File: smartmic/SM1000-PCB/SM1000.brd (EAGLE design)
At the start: 125 x 100 mm, 140 parts, among them CN1 HDR100-6, CN2 MOLEX-MINI-B-SMT, CN3 RASM712PX, CN4 RJ-45, CN5 MJ-3523-SMT, CN6 MJ-3523-SMT, CN7 MJ-3523-SMT, CN8 MJ-3523-SMT, CN9 MJ-3523-SMT, IC1 DIL-16, J1 JMP-2PIN, J2 JMP-2PIN, J3 JMP-2PIN, J4 JMP-2PIN, J5 JMP-2PIN, Q1 MMBT4401, Q2 MMBT4401, SW1 SW-SPST-2-1437565-0, SW2 SW-SPST-2-1437565-0, SW3 DPDT, T1 LM-NP-1001-B1L, T2 LM-NP-1001-B1L, U1 STM32F407, U2 LD3985M33R, U3 STMPS2141, U4 EMIF02-USB03F2, U5 TPS54329E, U6 LMV341, U7 LMV341, U8 LM386M-1, X1 8.0MHz

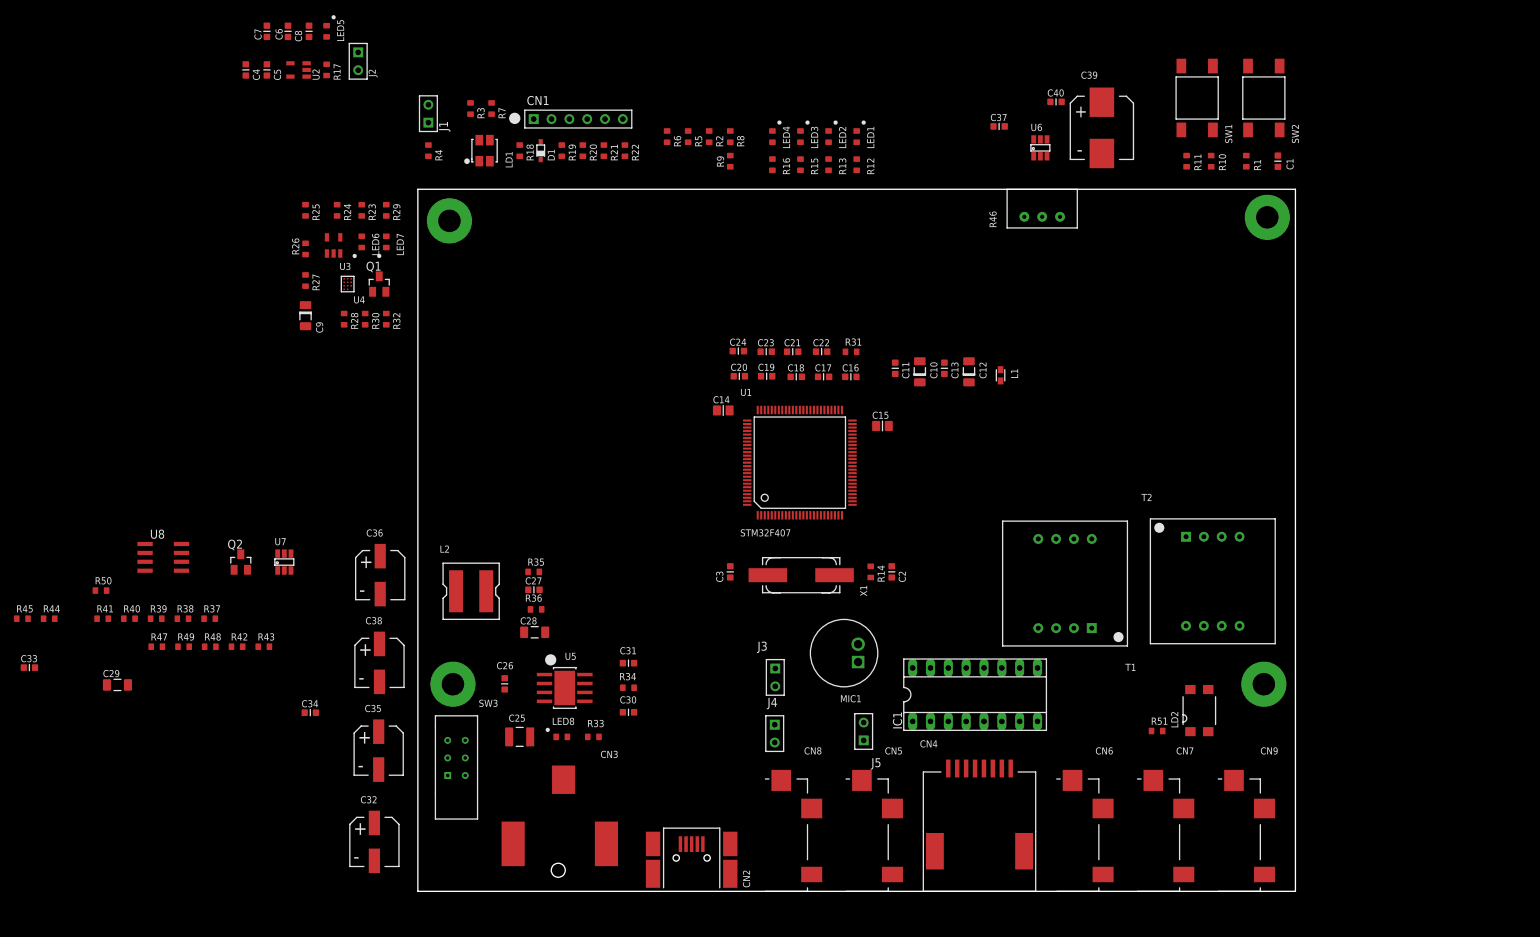
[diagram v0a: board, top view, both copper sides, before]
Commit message: 
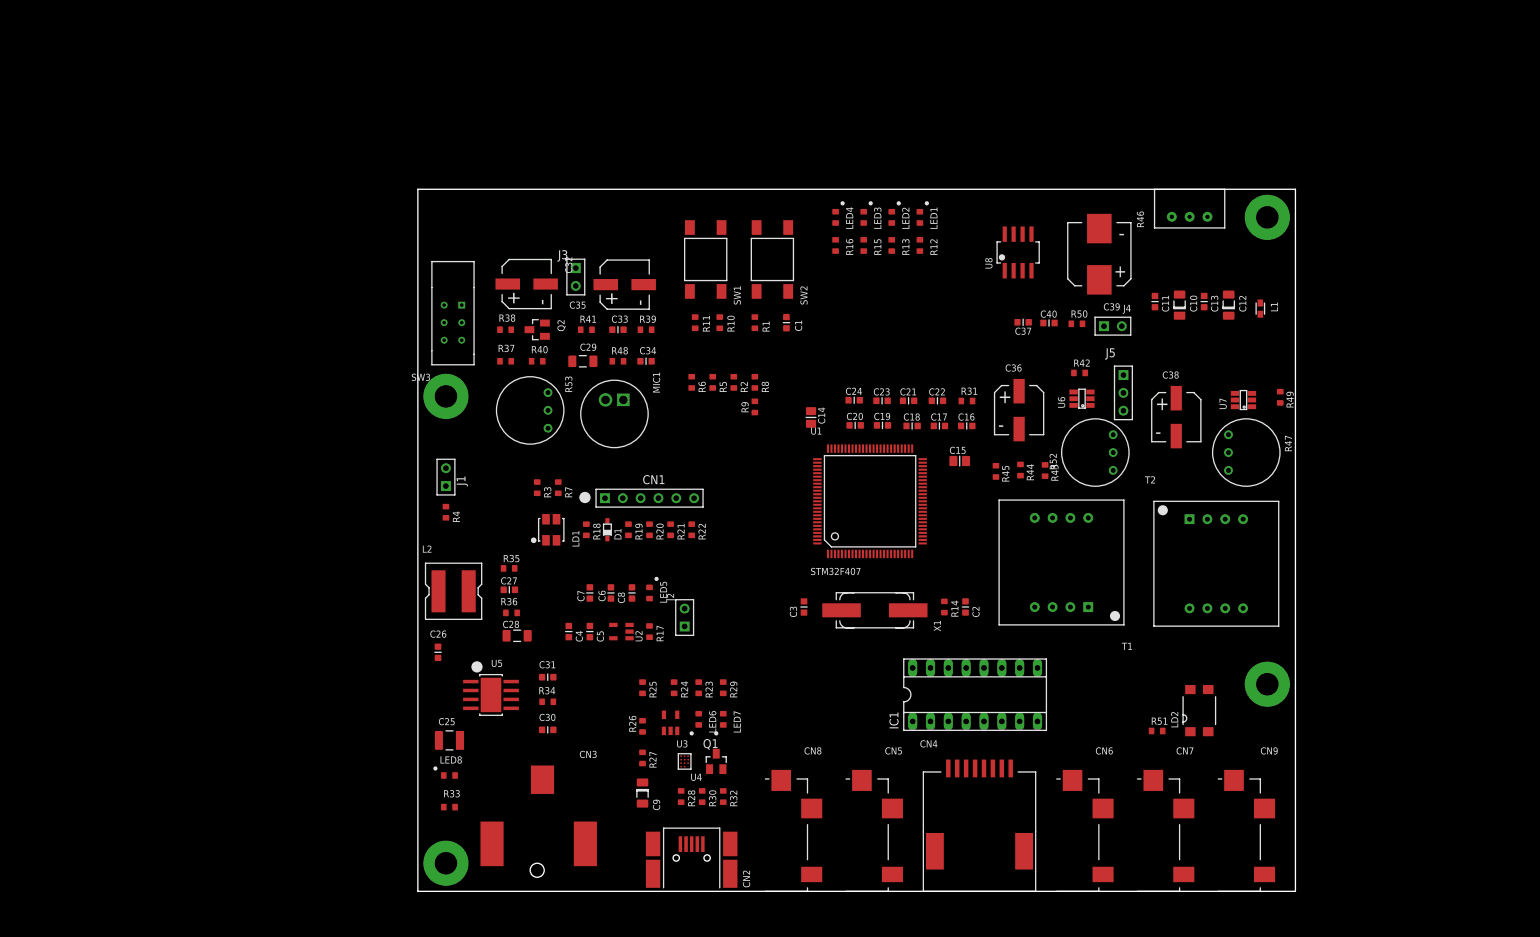
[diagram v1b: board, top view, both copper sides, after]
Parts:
- added R52: 10K, _RoweTel:TRIMPOT91
- added R53: TRIMPOT91, _RoweTel:TRIMPOT91
- added SH4: SHUNT,0.1IN, _Coherix:NOPACKAGE
- J5: value JMP-2PIN -> JMPR-3PIN; device _Coherix:JMPR-2PIN -> _Coherix:JMPR-3PIN
- LED1: value LED-GRN -> LED-RED
- LED2: value LED-ORG -> LED-RED
- LED3: value LED-RED -> LED-GRN
- LED4: value LED-BLU -> LED-YEL
- R42: value 4.99K,1% -> 10K,1%
- R47: value 100K,1% -> 100K; device _RoweTel:R0603 -> _RoweTel:TRIMPOT91
- U8: device AA-IC:SO08 -> _RoweTel:SO08
- moved R49 160.2 mm to (122.8, 70.4), turned to 270 degrees
- moved R47 157.6 mm to (118.0, 62.5), turned to 270 degrees
- moved R50 144.1 mm to (93.9, 80.8)
- moved R45 140.2 mm to (82.3, 59.8), turned to 270 degrees
- moved R44 140.0 mm to (85.8, 60.0), turned to 270 degrees
- moved U7 138.6 mm to (117.6, 70.0), turned to 90 degrees
- moved U8 129.3 mm to (85.5, 91.0), turned to 0 degrees
- moved R42 126.2 mm to (94.2, 73.8)
- moved C38 118.8 mm to (108.0, 67.5)
- moved R43 114.1 mm to (89.3, 59.9), turned to 270 degrees
- moved C33 96.7 mm to (28.5, 80.0), turned to 180 degrees
- moved C36 94.0 mm to (85.6, 68.5)
- moved J2 93.0 mm to (38.0, 39.0), turned to 180 degrees
- moved C4 92.3 mm to (21.5, 37.0)
- moved C5 92.3 mm to (24.5, 37.0)
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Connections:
- net LED-BLU renamed LED-ERR
- net LED-GRN renamed LED-PWR
- net LED-ORG renamed LED-PTT
- net LED-RED renamed LED-RT
- new net N$48: R42.1, R52.3, U6.4
- new net N$60: CN5.10, J5.2
- net AIN2: now also R52.2; no longer R42.1, U6.4
- net GND: now also J5.3, R52.1; no longer J5.2
- net N$32: no longer CN5.10
- net N$90: now also R47.3
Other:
- board text added: "AUX INP"
- board text added: "ERROR LED"
- board text added: "EXT MIC"
- board text added: "EXT SPKR"
- board text added: "EXT SPKR AMP"
- board text added: "MIC"
- board text added: "MIC INTF."
- board text added: "MIC PREAMP"
- board text added: "OTG USB"
- board text added: "PTT"
- board text added: "PTT LED"
- board text added: "PWR IN"
- board text added: "PWR LED"
- board text added: "PWR SW"
- board text added: "RCVR LEV"
- board text added: "SPEAKER INTF."
- board text added: "SPKR"
- board text added: "SPKR LEV"
- board text added: "USB INTF"

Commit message: SM1000
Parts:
- removed J4: JMP-2PIN, _Coherix:JMPR-2PIN
- added C41, C42, C43, C45: 100nF,16V, _RoweTel:C0603
- added C44: 100nf,16V, _RoweTel:C0603
- added FB1, FB2, FB3, FB4, FB6: FB0805, _RoweTel:FE0805
- added FB5: FB1210, _RoweTel:FE1210
- added R54: 1K,1%, _RoweTel:R0603
- C22, C23: device _Coherix:C0603 -> _RoweTel:C0603
- LED1, LED2, LED3, LED4: device _Coherix:CHIP-LED-0603 -> _RoweTel:LTST-S2200K
- R53: value TRIMPOT91 -> 10K
- T1, T2: value LM-NP-1001-B1L -> SM-LP-5001; device _RoweTel:LM-NP-1001-B1L -> _RoweTel:SM-LP-5001
- moved C22 83.3 mm to (-8.00, 55.0)
- moved C29 71.9 mm to (-13.0, 13.5)
- moved C32 71.9 mm to (-21.0, 24.5)
- moved C33 71.9 mm to (-8.00, 18.0)
- moved C34 71.9 mm to (-4.00, 13.5)
- moved C35 71.9 mm to (-7.04, 24.4)
- moved J3 71.9 mm to (-14.0, 25.5)
- moved MIC1 71.9 mm to (-8.50, 6.00)
- moved Q2 71.9 mm to (-19.5, 18.0)
- moved R37 71.9 mm to (-24.0, 13.5)
- moved R38 71.9 mm to (-24.0, 18.0)
- moved R39 71.9 mm to (-4.00, 18.0)
- moved R40 71.9 mm to (-19.5, 13.5)
- moved R41 71.9 mm to (-12.5, 18.0)
- moved R48 71.9 mm to (-8.00, 13.5)
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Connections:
- removed net N$37: C25.1, R33.1, R34.1, SW3.6, U5.2
- new net N$70: Q2.3, R38.2, R40.1, R53.1
- new net N$72: CN7.2, FB2.2
- new net N$73: CN9.2, FB6.2
- new net N$74: FB6.1, LD2.4
- new net N$75: CN8.2, FB3.2
- new net N$76: CN5.2, FB4.1
- new net N$77: CN3.2, FB5.1
- new net N$78: FB5.2, SW3.5
- net +3.3V: no longer LD1.4
- net +5V: now also C22.1
- net +VIN: now also C23.1, C25.1, R33.1, R34.1, SW3.6, U5.2; no longer CN3.2, SW3.5
- net AIN2: now also R53.2; no longer Q2.3, R38.2, R40.1
- net GND: now also C41.2, C42.2, R53.3, R54.1, T1.3, T2.3; no longer J4.1, T1.5, T2.4
- net MIC: now also C44.1
- net N$25: now also FB4.2; no longer CN5.2
- net N$33: now also FB1.1, T1.6; no longer CN6.2, T1.1
- net N$44: now also FB3.1; no longer CN8.2
- net N$61: now also FB2.1, T2.6; no longer CN7.2, T2.8
- net N$63: now also R54.2, T1.1; no longer T1.8
- net N$64: now also CN6.2, FB1.2; no longer CN8.10, J4.2
- net PTT: now also C45.1; no longer LD2.4
- net RF: now also C43.2, C44.2, C45.2, T2.4; no longer T2.5
- net SPKR: now also C43.1
- net VDD: now also C41.1, C42.1, LD1.4; no longer C22.1, C23.1
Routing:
- net PTT: track 0.00 -> 44.8 mm, vias 0 -> 2
- net MIC: track 0.00 -> 38.5 mm, vias 0 -> 1
- net SPKR: track 0.00 -> 37.0 mm, vias 0 -> 1
- net N$61: track 0.00 -> 19.2 mm, vias 0 -> 2
- net GND: track 0.00 -> 14.9 mm, vias 0 -> 3
- net N$33: track 0.00 -> 14.6 mm, vias 0 -> 2
- net N$73: track 0.00 -> 13.1 mm, vias 0 -> 2
- net N$72: track 0.00 -> 10.0 mm
- net N$64: track 0.00 -> 9.10 mm
- net N$51: track 0.00 -> 8.95 mm
- net N$58: track 0.00 -> 8.65 mm
- net STLINK: track 0.00 -> 8.17 mm
- net N$52: track 0.00 -> 7.84 mm
- net N$57: track 0.00 -> 6.96 mm
- net N$53: track 0.00 -> 6.14 mm
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- added copper zone on layer 1, net GND
- added copper zone on layer 15, net GND
- added copper zone on layer 1, net RF
- added copper zone on layer 2, net VDD
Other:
- board size 125 x 100 mm -> 100 x 80 mm
- board text removed: "EXT SPKR AMP"
- board text removed: "LED1-4"
- board text removed: "MIC PREAMP"

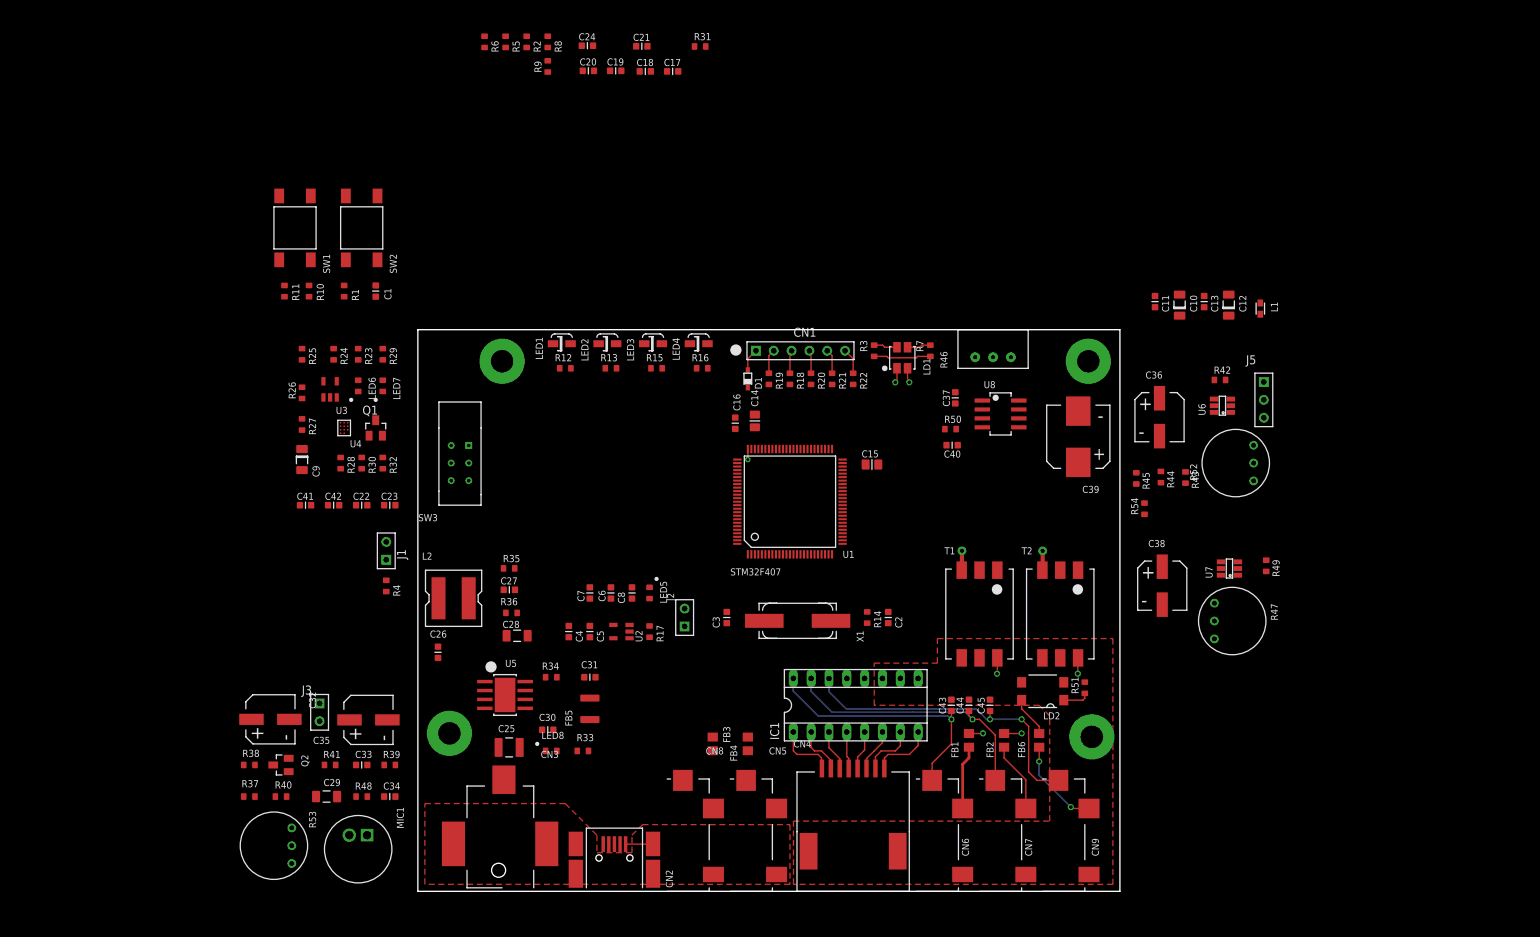
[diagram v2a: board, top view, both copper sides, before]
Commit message: 
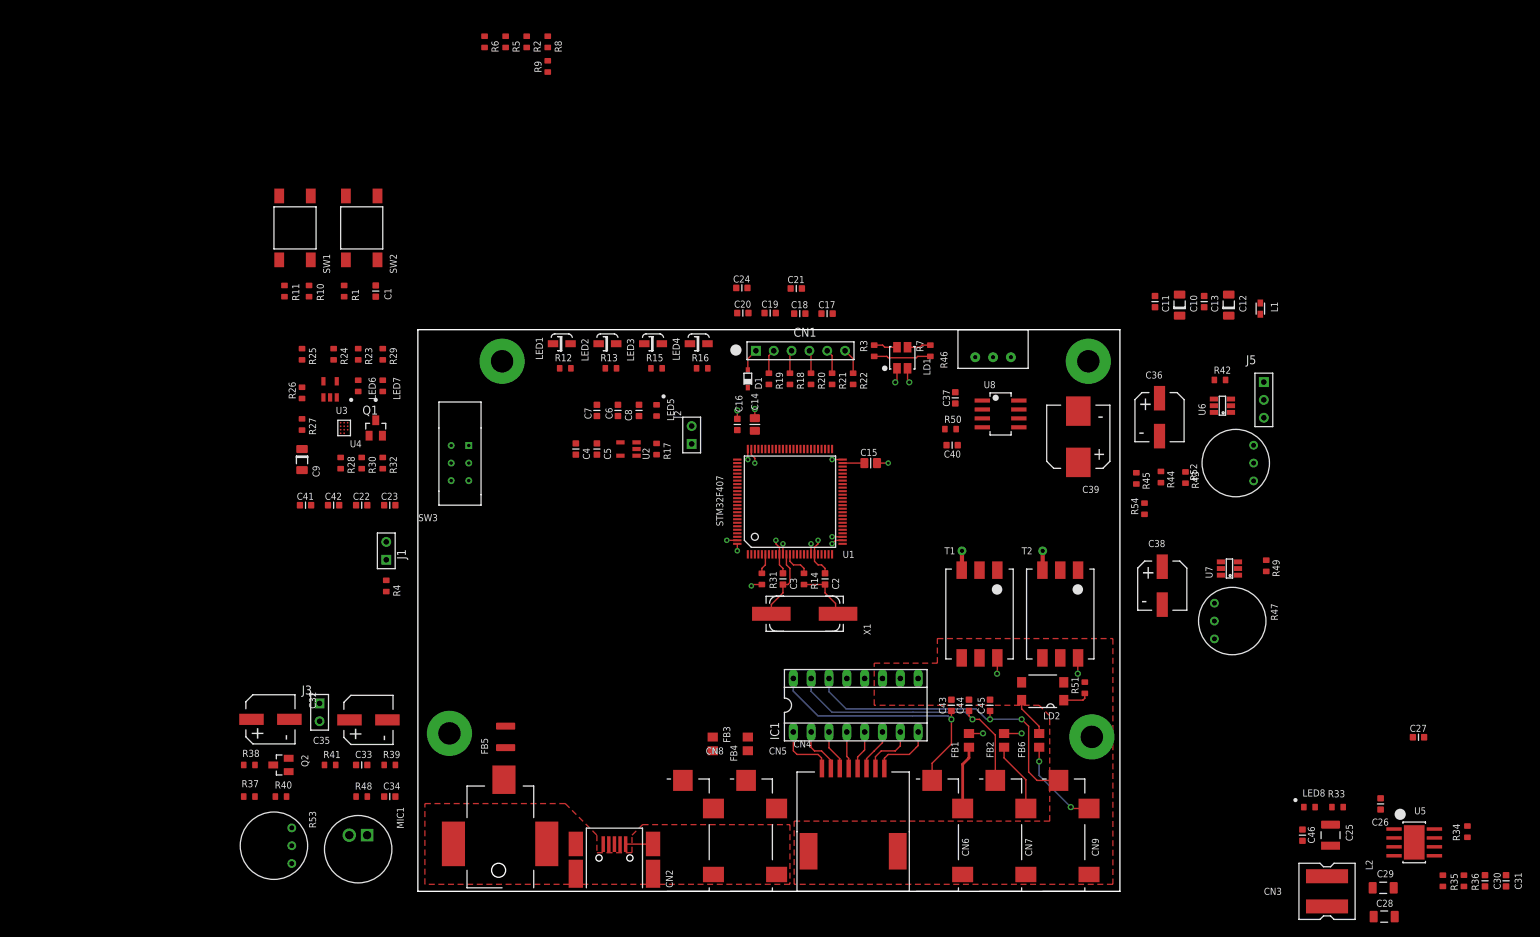
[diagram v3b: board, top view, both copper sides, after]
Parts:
- added C46: 100nF,25V, _RoweTel:C0603
- C44: value 100nf,16V -> 100nF,16V
- moved C29 151.1 mm to (137.5, 0.50)
- moved R36 140.9 mm to (149.0, 1.50), turned to 270 degrees
- moved R35 140.2 mm to (146.0, 1.50), turned to 90 degrees
- moved C26 136.0 mm to (137.1, 12.4), turned to 90 degrees
- moved C30 135.2 mm to (152.0, 1.50), turned to 270 degrees
- moved C31 133.7 mm to (155.0, 1.50), turned to 270 degrees
- moved R34 132.3 mm to (149.5, 8.50), turned to 270 degrees
- moved L2 131.2 mm to (129.5, 0.00), turned to 270 degrees
- moved C27 131.2 mm to (142.5, 21.9)
- moved U5 131.2 mm to (141.9, 6.97)
- moved C28 129.8 mm to (137.6, -3.60)
- moved C25 117.7 mm to (130.0, 8.00), turned to 270 degrees
- moved LED8 108.3 mm to (127.0, 12.0)
- moved R33 107.8 mm to (131.0, 12.0)
- moved R31 76.3 mm to (49.0, 44.5), turned to 90 degrees
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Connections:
- net +VIN: now also C46.1
- net GND: now also C46.2
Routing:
- net GND: track 14.9 -> 35.3 mm, vias 3 -> 11
- net OSC_IN: track 0.00 -> 10.2 mm
- net VDD: track 3.60 -> 12.2 mm, vias 2 -> 8
- net N$10: track 0.00 -> 7.94 mm
- net OSC_OUT: track 0.00 -> 4.11 mm
- net N$3: track 0.00 -> 3.10 mm
- net N$2: track 0.00 -> 2.91 mm
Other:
- board text removed: "CRYSTAL"
- board text removed: "STLINK"
